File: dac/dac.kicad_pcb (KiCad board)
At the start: 2 copper layers, 24.1 x 37.1 mm, 35 parts, among them J1 Conn_01x14, U1 74LVC3G17, U2 74LVC3G17, U3 74LVC3G17

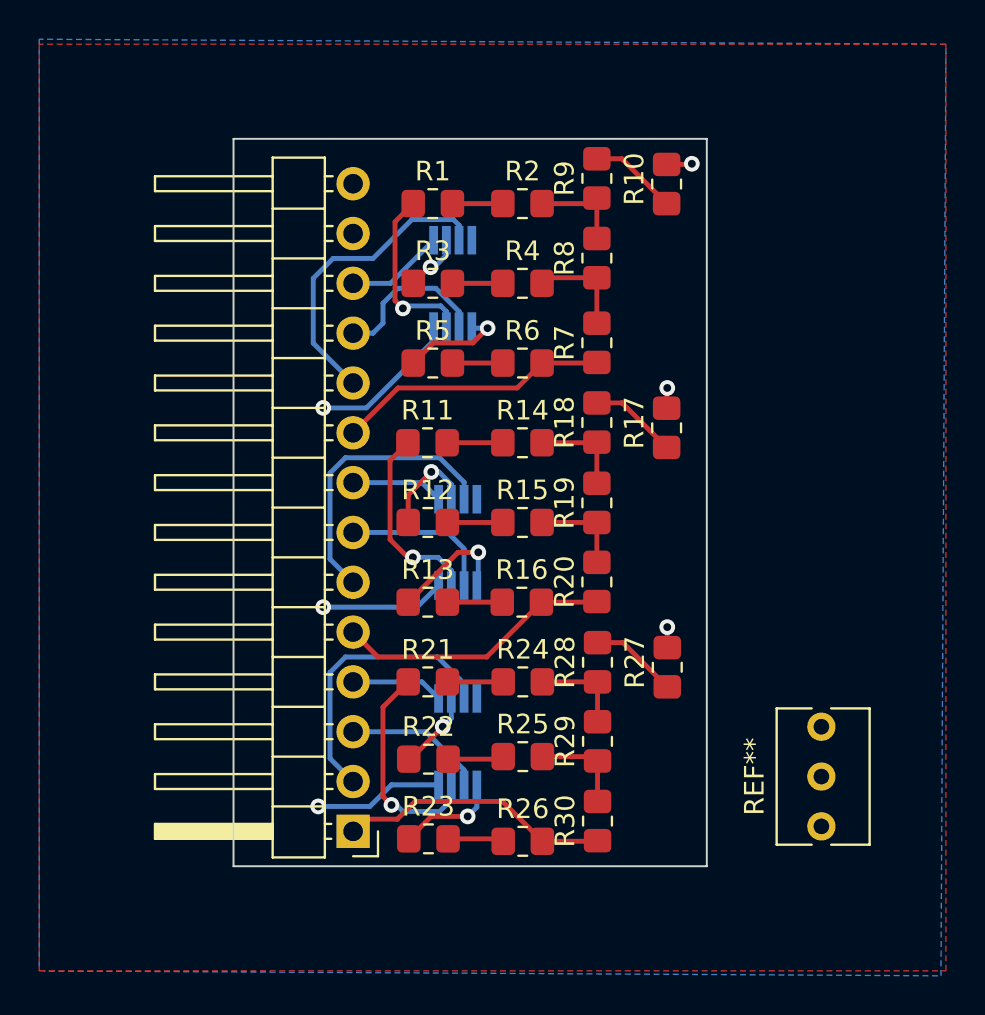
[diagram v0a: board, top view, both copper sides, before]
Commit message: timing board updates and adding keyboard loft board and vga breakout
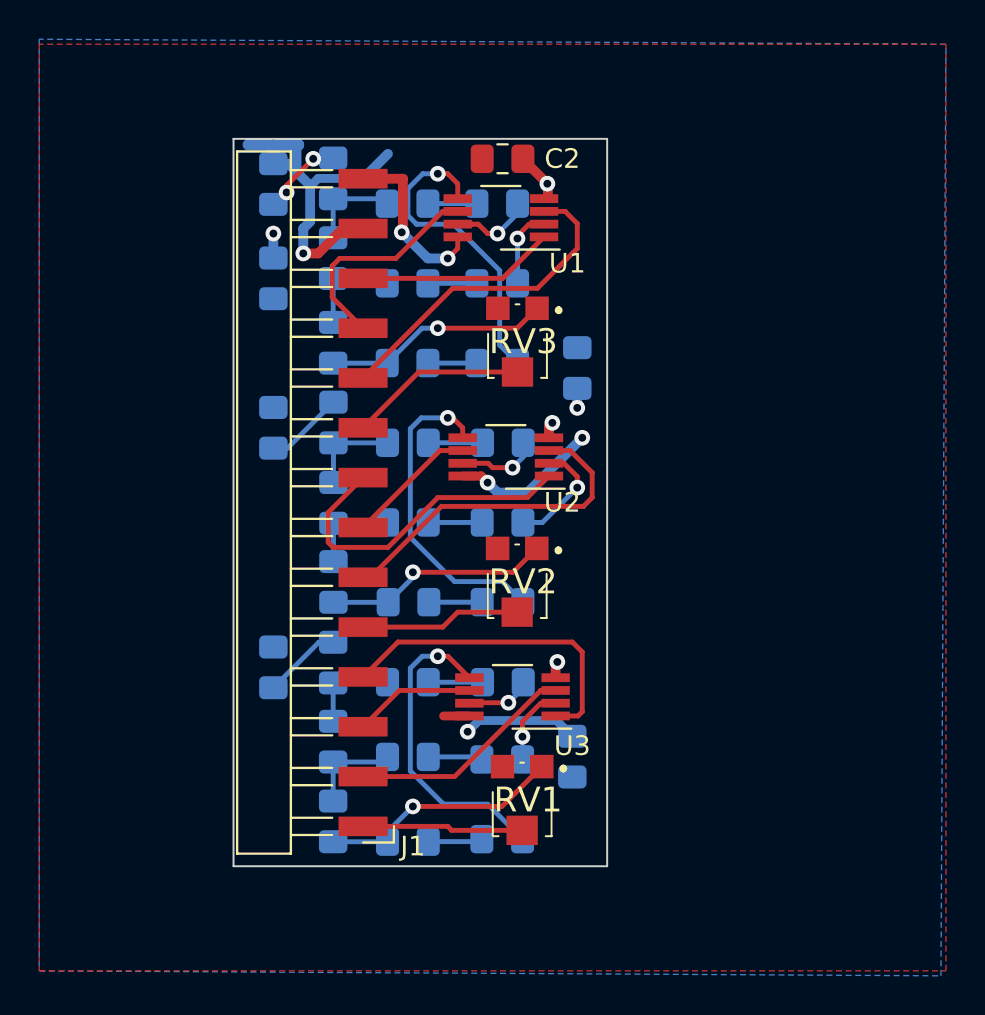
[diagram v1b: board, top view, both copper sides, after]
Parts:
- removed REF**: Potentiometer_Bourns_3266Y_Vertical, Potentiometer_THT:Potentiometer_Bourns_3266Y_Vertical
- added C1: 10u, Capacitor_SMD:C_0805_2012Metric_Pad1.18x1.45mm_HandSolder, B.Cu at (125.5, 88.6)
- added C2: 100n, Capacitor_SMD:C_0805_2012Metric_Pad1.18x1.45mm_HandSolder, F.Cu at (137.2, 82.5)
- added C3: 100n, Capacitor_SMD:C_0805_2012Metric_Pad1.18x1.45mm_HandSolder, B.Cu at (141.0, 93.2)
- added C4: 100n, Capacitor_SMD:C_0805_2012Metric_Pad1.18x1.45mm_HandSolder, B.Cu at (140.7, 113.0)
- added RV1: R_Potentiometer_Trim, local:TC33X2304E, F.Cu at (138.2, 115.3)
- added RV2: R_Potentiometer_Trim, local:TC33X2304E, F.Cu at (137.9, 104.2)
- added RV3: R_Potentiometer_Trim, local:TC33X2304E, F.Cu at (137.9, 92.0)
- J1: footprint Connector_PinHeader_2.54mm:PinHeader_1x14_P2.54mm_Horizontal -> Connector_Harwin:Harwin_M20-89014xx_1x14_P2.54mm_Horizontal
- R1, R10, R11, R12, R13, R14, R15, R16, R17, R18, R19, R2, R20, R21, R22, R23, R24, R25, R26, R27, R28, R29, R3, R30, R4, R5, R6, R7, R8, R9: footprint Resistor_SMD:R_0805_2012Metric_Pad1.20x1.40mm_HandSolder -> Capacitor_SMD:C_0805_2012Metric_Pad1.18x1.45mm_HandSolder; moved to B.Cu
- U1, U2, U3: moved to F.Cu
- moved R27 20.1 mm to (125.5, 108.5)
- moved R10 20.1 mm to (125.5, 83.8)
- moved R17 20.1 mm to (125.5, 96.3)
- moved J1 17.5 mm to (124.5, 100.1)
- moved R29 13.5 mm to (128.5, 112.3)
- moved R30 13.5 mm to (128.5, 116.3)
- moved R28 13.5 mm to (128.5, 108.2)
- moved R8 13.4 mm to (128.5, 87.6)
- moved R7 13.4 mm to (128.5, 91.9)
- moved R9 13.4 mm to (128.5, 83.5)
- moved R18 13.4 mm to (128.5, 96.0)
- moved R19 13.4 mm to (128.5, 100.1)
- moved R20 13.4 mm to (128.5, 104.1)
- moved R24 5.86 mm to (132.3, 109.2), turned to 180 degrees
- moved R25 5.86 mm to (132.3, 113.0), turned to 180 degrees
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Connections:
- R16 pad 2: /Green -> Net-(R16-Pad2)
- R20 pad 1: /Green -> Net-(R16-Pad2)
- R26 pad 2: /Blue -> Net-(R26-Pad2)
- R30 pad 1: /Blue -> Net-(R26-Pad2)
- R6 pad 2: /Red -> Net-(R6-Pad2)
- R7 pad 1: /Red -> Net-(R6-Pad2)
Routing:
- net GND: track 3.39 -> 23.9 mm, vias 3 -> 4
- net Net-(R26-Pad2): track 0.00 -> 12.5 mm, vias 0 -> 1
- net /G0: track 4.71 -> 16.9 mm
- net /B0: track 4.71 -> 16.6 mm
- net Net-(R16-Pad2): track 0.00 -> 11.7 mm, vias 0 -> 1
- net Net-(R6-Pad2): track 0.00 -> 11.6 mm, vias 0 -> 1
- net Net-(R23-Pad1): track 5.28 -> 16.1 mm
- net Net-(R5-Pad1): track 5.37 -> 16.1 mm
- net Net-(R13-Pad1): track 6.35 -> 16.3 mm
- net Net-(R21-Pad1): track 11.2 -> 3.36 mm
- net /Green: track 14.1 -> 8.17 mm
- net /Blue: track 13.9 -> 8.20 mm
- net Net-(R11-Pad1): track 9.85 -> 4.13 mm
- net VCC: track 20.7 -> 26.1 mm, vias 3 -> 7
- net /R0: track 5.02 -> 10.1 mm
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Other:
- board size 24.1 x 37.1 mm -> 19 x 37.1 mm

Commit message: current boards
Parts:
- added C10: 100n, Capacitor_SMD:C_0805_2012Metric_Pad1.18x1.45mm_HandSolder, F.Cu at (140.2, 111.8)
- added C5: 100n, Capacitor_SMD:C_0805_2012Metric_Pad1.18x1.45mm_HandSolder, F.Cu at (139.9, 89.7)
- added C6: 100n, Capacitor_SMD:C_0805_2012Metric_Pad1.18x1.45mm_HandSolder, F.Cu at (140.0, 93.0)
- added C7: 100n, Capacitor_SMD:C_0805_2012Metric_Pad1.18x1.45mm_HandSolder, F.Cu at (135.4, 95.5)
- added C8: 100n, Capacitor_SMD:C_0805_2012Metric_Pad1.18x1.45mm_HandSolder, F.Cu at (140.2, 102.9)
- added C9: 100n, Capacitor_SMD:C_0805_2012Metric_Pad1.18x1.45mm_HandSolder, F.Cu at (140.2, 109.2)
- added U4: 74AHCT1G125, Package_TO_SOT_SMD:SOT-353_SC-70-5_Handsoldering, F.Cu at (135.4, 92.6)
- added U5: 74AHCT1G125, Package_TO_SOT_SMD:SOT-353_SC-70-5_Handsoldering, F.Cu at (135.4, 98.3)
- added U6: 74AHCT1G125, Package_TO_SOT_SMD:SOT-353_SC-70-5_Handsoldering, F.Cu at (135.4, 102.1)
- added U7: 74AHCT1G125, Package_TO_SOT_SMD:SOT-353_SC-70-5_Handsoldering, F.Cu at (135.4, 105.6)
- added U8: 74AHCT1G125, Package_TO_SOT_SMD:SOT-353_SC-70-5_Handsoldering, F.Cu at (135.4, 108.9)
- added U9: 74AHCT1G125, Package_TO_SOT_SMD:SOT-353_SC-70-5_Handsoldering, F.Cu at (135.4, 111.9)
- C3, C4: moved to F.Cu
- U1, U2, U3: value 74LVC3G17 -> 74AHCT1G125; footprint Package_SO:VSSOP-8_3.0x3.0mm_P0.65mm -> Package_TO_SOT_SMD:SOT-353_SC-70-5_Handsoldering
- moved C2 23.6 mm to (140.2, 105.9)
- moved U3 20.7 mm to (135.3, 89.4), turned to 0 degrees
- moved U2 19.5 mm to (135.4, 117.2), turned to 0 degrees
- moved C3 11.7 mm to (135.1, 83.1), turned to 180 degrees
- moved RV3 7.66 mm to (140.2, 84.7)
- moved RV2 6.14 mm to (140.5, 98.6)
- moved C4 5.57 mm to (135.4, 114.6), turned to 180 degrees
- moved RV1 2.37 mm to (140.5, 115.9)
- moved U1 1.80 mm to (135.3, 86.0), turned to 0 degrees
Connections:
- R1 pad 1: Net-(R1-Pad1) -> /Rb0
- R11 pad 1: Net-(R11-Pad1) -> /Gb0
- R12 pad 1: Net-(R12-Pad1) -> /Gb1
- R13 pad 1: Net-(R13-Pad1) -> /Gb2
- R21 pad 1: Net-(R21-Pad1) -> /Bb0
- R22 pad 1: Net-(R22-Pad1) -> /Bb1
- R23 pad 1: Net-(R23-Pad1) -> /Bb2
- R3 pad 1: Net-(R3-Pad1) -> /Rb1
- R5 pad 1: Net-(R5-Pad1) -> /Rb2
- U1 pad 1: /R0 -> GND
- U1 pad 2: Net-(R3-Pad1) -> /R0
- U1 pad 3: /R2 -> GND
- U1 pad 4: GND -> /Rb0
- U1 pad 5: Net-(R5-Pad1) -> VCC
- U2 pad 1: /G0 -> GND
- U2 pad 2: Net-(R12-Pad1) -> /B2
- U2 pad 3: /G2 -> GND
- U2 pad 4: GND -> /Bb2
- U2 pad 5: Net-(R13-Pad1) -> VCC
- U3 pad 1: /B0 -> GND
- U3 pad 2: Net-(R22-Pad1) -> /R1
- U3 pad 3: /B2 -> GND
- U3 pad 4: GND -> /Rb1
- U3 pad 5: Net-(R23-Pad1) -> VCC
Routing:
- net GND: track 23.9 -> 107.8 mm, vias 4 -> 18
- net VCC: track 26.1 -> 60.2 mm
- net Net-(R13-Pad1): track 16.3 -> 0.00 mm, vias 1 -> 0
- net Net-(R5-Pad1): track 16.1 -> 0.00 mm, vias 1 -> 0
- net Net-(R23-Pad1): track 16.1 -> 0.00 mm, vias 1 -> 0
- net /Red: track 9.05 -> 23.8 mm, vias 0 -> 2
- net /Green: track 8.17 -> 22.7 mm
- net /G0: track 16.9 -> 4.21 mm
- net /G2: track 17.3 -> 4.75 mm
- net /B0: track 16.6 -> 4.11 mm
- net /R2: track 16.9 -> 4.48 mm
- net Net-(R6-Pad2): track 11.6 -> 21.2 mm
- net /R1: track 11.4 -> 4.69 mm
- net Net-(R16-Pad2): track 11.7 -> 17.9 mm
- net Net-(R12-Pad1): track 5.79 -> 0.00 mm, vias 1 -> 0
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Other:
- board size 19 x 37.1 mm -> 21.1 x 37.1 mm
- board text added: "Blue DAC"
- board text added: "Green DAC"
- board text added: "Red DAC"
